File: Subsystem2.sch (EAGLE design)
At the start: 22 parts

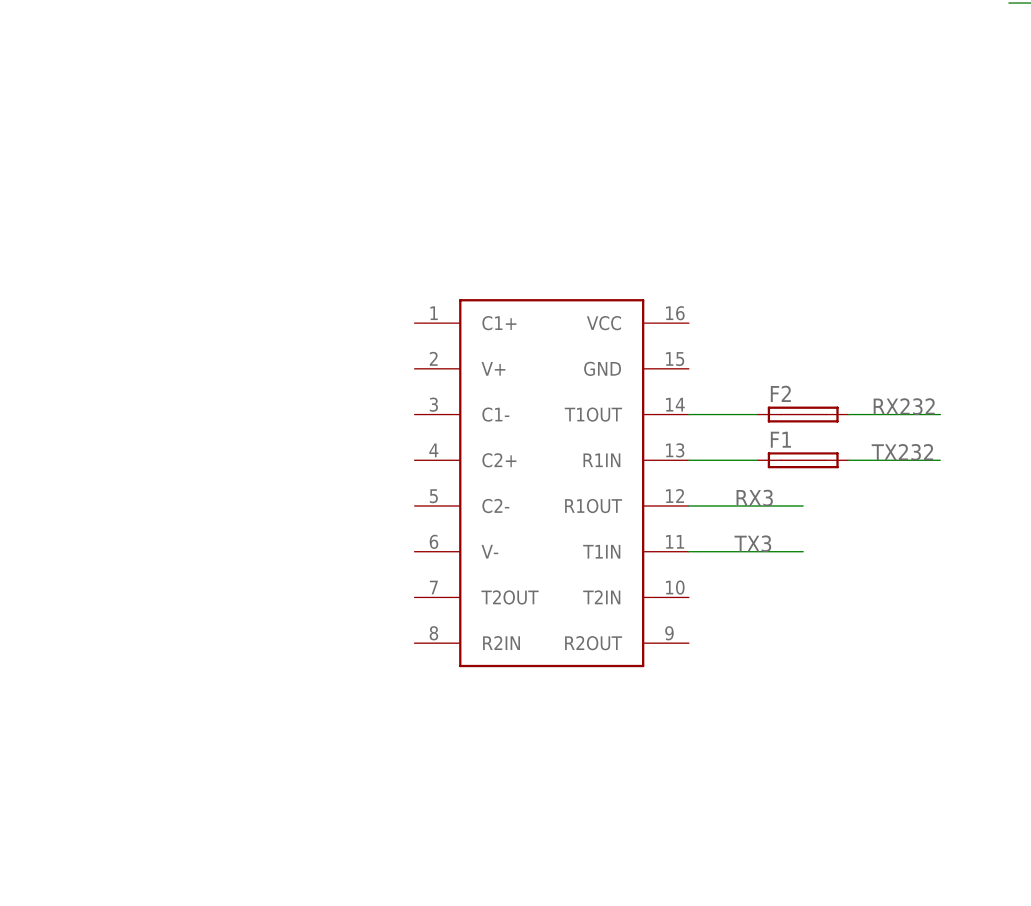
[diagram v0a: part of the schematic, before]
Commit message: add 3232 external caps
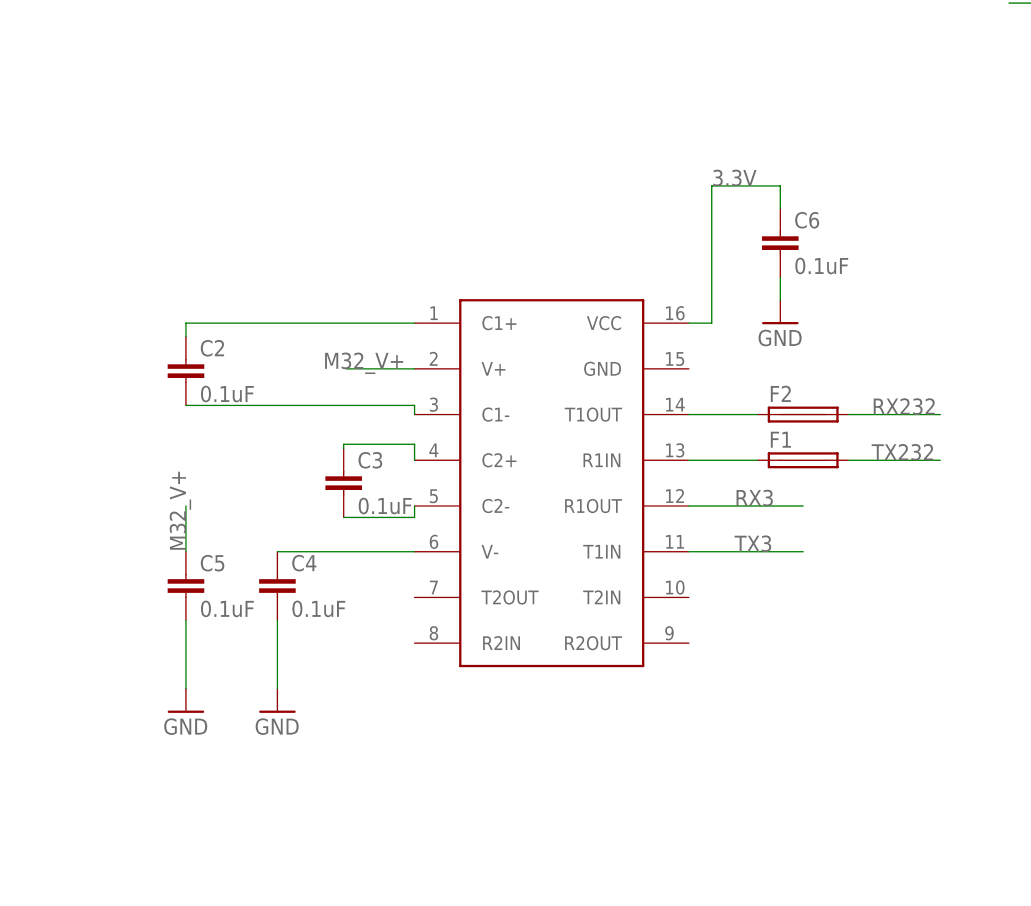
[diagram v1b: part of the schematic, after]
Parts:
- added C2, C3, C4, C5, C6: 0.1uF, Brendan:CAP0805
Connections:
- new net M32_C1+: C2.1, U$2.C1+
- new net M32_C1-: C2.2, U$2.C1-
- new net M32_C2+: C3.1, U$2.C2+
- new net M32_C2-: C3.2, U$2.C2-
- new net M32_V+: C5.1, U$2.V+
- new net M32_V-: C4.1, U$2.V-
- net 3.3V: now also C6.1, U$2.VCC
- net GND: now also C4.2, C5.2, C6.2
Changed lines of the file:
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@@
 <part name="F1" library="Brendan" deviceset="TE5" device=""/>
 <part name="F2" library="Brendan" deviceset="TE5" device=""/>
+<part name="C2" library="Brendan" deviceset="CAP" device="0805" value="0.1uF"/>
+<part name="C3" library="Brendan" deviceset="CAP" device="0805" value="0.1uF"/>
+<part name="C4" library="Brendan" deviceset="CAP" device="0805" value="0.1uF"/>
+<part name="C5" library="Brendan" deviceset="CAP" device="0805" value="0.1uF"/>
+<part name="GND4" library="supply1" deviceset="GND" device=""/>
+<part name="GND5" library="supply1" deviceset="GND" device=""/>
+<part name="C6" library="Brendan" deviceset="CAP" device="0805" value="0.1uF"/>
+<part name="GND6" library="supply1" deviceset="GND" device=""/>
 </parts>
 <sheets>
@@
 <instance part="F1" gate="1" x="139.7" y="-22.86"/>
 <instance part="F2" gate="1" x="139.7" y="-17.78"/>
+<instance part="C2" gate="G$1" x="71.12" y="-14.224"/>
+<instance part="C3" gate="G$1" x="88.646" y="-26.67"/>
+<instance part="C4" gate="G$1" x="81.28" y="-38.1"/>
+<instance part="C5" gate="G$1" x="71.12" y="-38.1"/>
+<instance part="GND4" gate="1" x="71.12" y="-50.8"/>
+<instance part="GND5" gate="1" x="81.28" y="-50.8"/>
+<instance part="C6" gate="G$1" x="137.16" y="0"/>
+<instance part="GND6" gate="1" x="137.16" y="-7.62"/>
 </instances>
 <busses>
@@
 <label x="193.04" y="167.64" size="1.778" layer="95"/>
 </segment>
+<segment>
+<pinref part="C5" gate="G$1" pin="2"/>
+<wire x1="71.12" y1="-40.64" x2="71.12" y2="-48.26" width="0.1524" layer="91"/>
+<pinref part="GND4" gate="1" pin="GND"/>
+</segment>
+<segment>
+<pinref part="C4" gate="G$1" pin="2"/>
+<wire x1="81.28" y1="-40.64" x2="81.28" y2="-48.26" width="0.1524" layer="91"/>
+<pinref part="GND5" gate="1" pin="GND"/>
+</segment>
+<segment>
+<pinref part="C6" gate="G$1" pin="2"/>
+<wire x1="137.16" y1="-2.54" x2="137.16" y2="-5.08" width="0.1524" layer="91"/>
+<pinref part="GND6" gate="1" pin="GND"/>
+</segment>
 </net>
 <net name="N$4" class="0">
@@
 <wire x1="152.4" y1="172.72" x2="139.7" y2="172.72" width="0.1524" layer="91"/>
 <label x="144.78" y="172.72" size="1.778" layer="95"/>
+</segment>
+<segment>
+<pinref part="U$2" gate="G$1" pin="VCC"/>
+<wire x1="127" y1="-7.62" x2="129.54" y2="-7.62" width="0.1524" layer="91"/>
+<wire x1="129.54" y1="-7.62" x2="129.54" y2="7.62" width="0.1524" layer="91"/>
+<wire x1="129.54" y1="7.62" x2="137.16" y2="7.62" width="0.1524" layer="91"/>
+<pinref part="C6" gate="G$1" pin="1"/>
+<wire x1="137.16" y1="7.62" x2="137.16" y2="5.08" width="0.1524" layer="91"/>
+<label x="129.54" y="7.62" size="1.778" layer="95"/>
 </segment>
 </net>
@@
 </segment>
 </net>
+<net name="M32_C1+" class="0">
+<segment>
+<pinref part="U$2" gate="G$1" pin="C1+"/>
+<wire x1="96.52" y1="-7.62" x2="71.12" y2="-7.62" width="0.1524" layer="91"/>
+<pinref part="C2" gate="G$1" pin="1"/>
+<wire x1="71.12" y1="-9.144" x2="71.12" y2="-7.62" width="0.1524" layer="91"/>
+</segment>
+</net>
+<net name="M32_C1-" class="0">
+<segment>
+<pinref part="C2" gate="G$1" pin="2"/>
+<pinref part="U$2" gate="G$1" pin="C1-"/>
+<wire x1="71.12" y1="-16.764" x2="96.52" y2="-16.764" width="0.1524" layer="91"/>
+<wire x1="96.52" y1="-16.764" x2="96.52" y2="-17.78" width="0.1524" layer="91"/>
+</segment>
+</net>
+<net name="M32_C2+" class="0">
+<segment>
+<pinref part="U$2" gate="G$1" pin="C2+"/>
+<wire x1="96.52" y1="-22.86" x2="96.52" y2="-21.082" width="0.1524" layer="91"/>
+<wire x1="96.52" y1="-21.082" x2="88.646" y2="-21.082" width="0.1524" layer="91"/>
+<pinref part="C3" gate="G$1" pin="1"/>
+<wire x1="88.646" y1="-21.082" x2="88.646" y2="-21.59" width="0.1524" layer="91"/>
+</segment>
+</net>
+<net name="M32_C2-" class="0">
+<segment>
+<pinref part="C3" gate="G$1" pin="2"/>
+<pinref part="U$2" gate="G$1" pin="C2-"/>
+<wire x1="88.646" y1="-29.21" x2="96.52" y2="-29.21" width="0.1524" layer="91"/>
+<wire x1="96.52" y1="-29.21" x2="96.52" y2="-27.94" width="0.1524" layer="91"/>
+</segment>
+</net>
+<net name="M32_V-" class="0">
+<segment>
+<pinref part="U$2" gate="G$1" pin="V-"/>
+<pinref part="C4" gate="G$1" pin="1"/>
+<wire x1="96.52" y1="-33.02" x2="81.28" y2="-33.02" width="0.1524" layer="91"/>
+</segment>
+</net>
+<net name="M32_V+" class="0">
+<segment>
+<pinref part="U$2" gate="G$1" pin="V+"/>
+<wire x1="96.52" y1="-12.7" x2="88.9" y2="-12.7" width="0.1524" layer="91"/>
+<label x="86.36" y="-12.7" size="1.778" layer="95"/>
+</segment>
+<segment>
+<pinref part="C5" gate="G$1" pin="1"/>
+<wire x1="71.12" y1="-33.02" x2="71.12" y2="-27.94" width="0.1524" layer="91"/>
+<label x="71.12" y="-33.02" size="1.778" layer="95" rot="R90"/>
+</segment>
+</net>

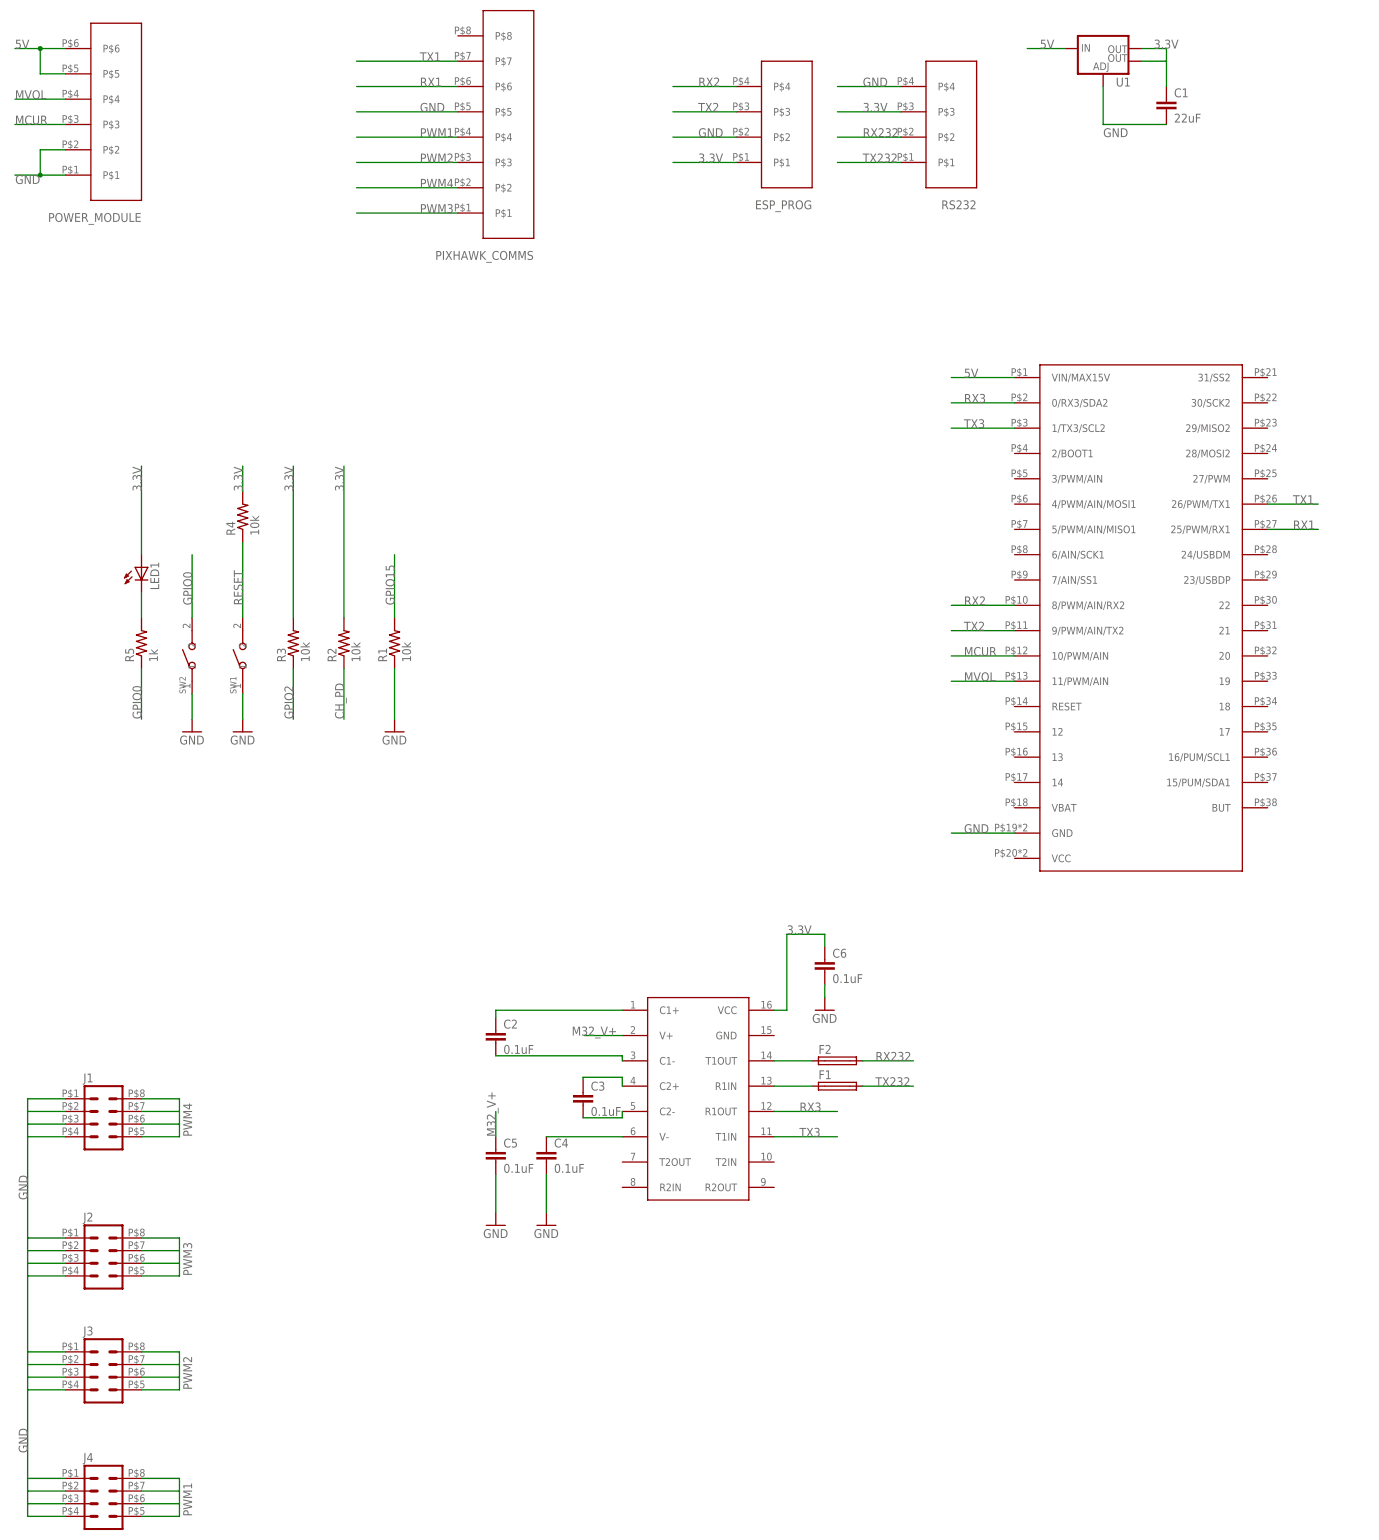
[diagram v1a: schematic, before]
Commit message: finish first-draft schematic of v2 board
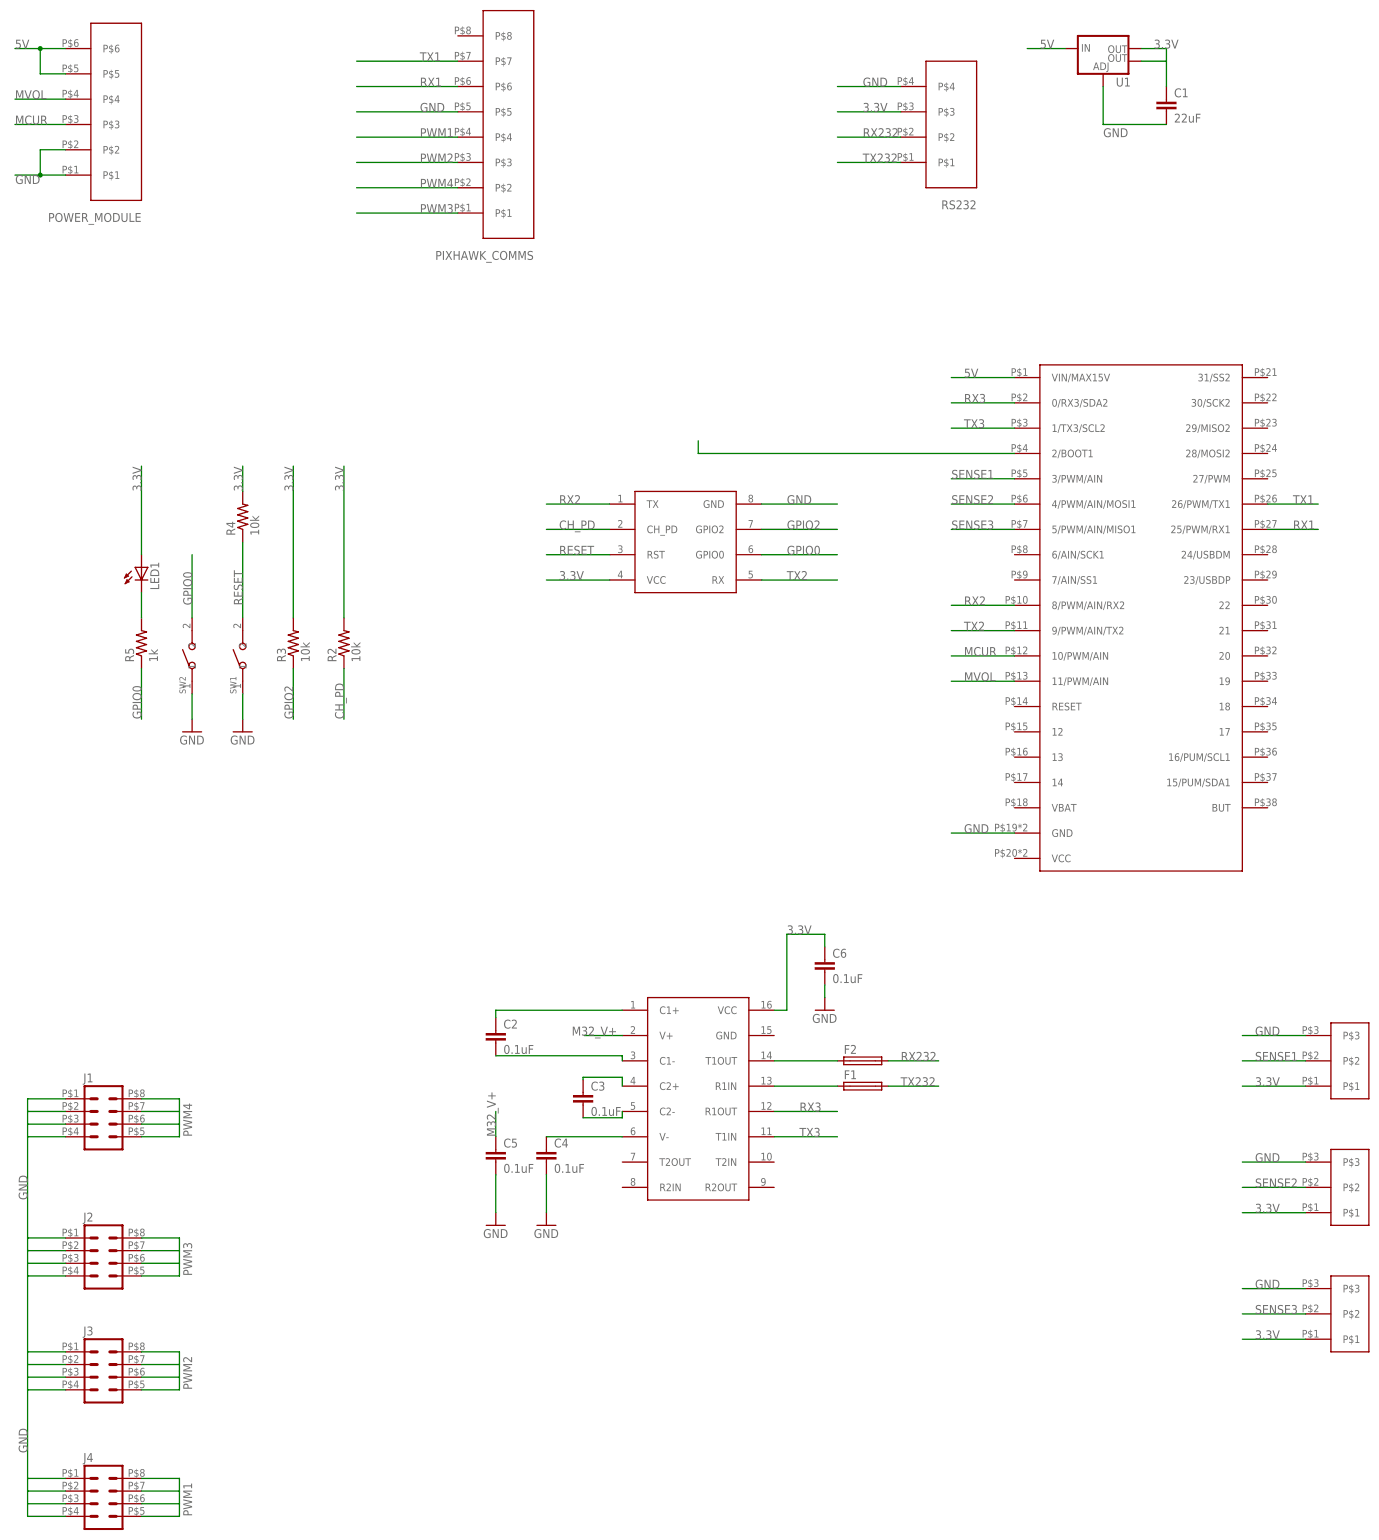
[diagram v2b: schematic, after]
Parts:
- removed ESP_PROG: 4PIN-PLUG, Brendan:4PIN-PLUG
- removed R1: 10k, Brendan:RESISTOR0805-RES
- added U$3: ESP-01, Brendan:ESP-01
- added U$4, U$5, U$6: 3PIN-PLUG, Brendan:3PIN-PLUG
- U$1: value MAPLE-MINI -> MAPLE-MINI-SOCKET; device Brendan:MAPLE-MINI -> Brendan:MAPLE-MINI-SOCKET
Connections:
- removed net GPIO15: R1.2
- new net N$5: U$1.2/BOOT1
- new net SENSE1: U$1.3/PWM/AIN, U$4.P$2
- new net SENSE2: U$1.4/PWM/AIN/MOSI1, U$5.P$2
- new net SENSE3: U$1.5/PWM/AIN/MISO1, U$6.P$2
- net 3.3V: now also U$3.VCC, U$4.P$1, U$5.P$1, U$6.P$1; no longer ESP_PROG.P$1
- net CH_PD: now also U$3.CH_PD
- net GND: now also U$3.GND, U$4.P$3, U$5.P$3, U$6.P$3; no longer ESP_PROG.P$2, R1.1
- net GPIO0: now also U$3.GPIO0
- net GPIO2: now also U$3.GPIO2
- net RESET: now also U$3.RST
- net RX2: now also U$3.TX; no longer ESP_PROG.P$4
- net TX2: now also U$3.RX; no longer ESP_PROG.P$3
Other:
- moved on the sheet: F1, F2
